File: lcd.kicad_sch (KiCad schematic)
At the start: 0 parts

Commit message: schema functionally done
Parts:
- added C18: 0.1uF, Capacitor_SMD:C_0805_2012Metric, symbol Device:C
- added C20: 1uF, Capacitor_SMD:C_0805_2012Metric, symbol Device:C
- added LCD1: LS013B7DH03, footprints:F3311A7H121010E200, symbol user:LS013B7DH03
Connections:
- new net: C20.1, LCD1.6 (VDDA), LCD1.7 (VDD), LCD1.8 (EXTMODE)
- new net: C18.1, LCD1.5 (DISP)
- new net GND: C18.2, C20.2, LCD1.10 (VSSA), LCD1.9 (VSS)
- new net LCD_COMIN: LCD1.4 (EXTCOMIN)
- new net LCD_SCLK: LCD1.1 (SCLK)
- new net LCD_SCS: LCD1.3 (SCS)
- new net LCD_SI: LCD1.2 (SI)
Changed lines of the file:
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@@
   (title_block
     (title "gkos pebble")
+    (date "2024-03-18")
+    (rev "1")
     (company "minteyay")
+    (comment 1 "memory LCD connection")
+  )
+  (junction (at 153.67 90.17) (diameter 0) (color 0 0 0 0)
+  )
+  (junction (at 157.48 121.92) (diameter 0) (color 0 0 0 0)
+  )
+  (junction (at 135.89 90.17) (diameter 0) (color 0 0 0 0)
+  )
+  (junction (at 135.89 121.92) (diameter 0) (color 0 0 0 0)
+  )
+  (junction (at 133.35 121.92) (diameter 0) (color 0 0 0 0)
+  )
+  (wire (pts (xy 133.35 90.17) (xy 135.89 90.17))
+    (stroke (width 0) (type default))
+  )
+  (wire (pts (xy 133.35 121.92) (xy 133.35 124.46))
+    (stroke (width 0) (type default))
+  )
+  (wire (pts (xy 153.67 107.95) (xy 149.86 107.95))
+    (stroke (width 0) (type default))
+  )
+  (wire (pts (xy 153.67 90.17) (xy 153.67 107.95))
+    (stroke (width 0) (type default))
+  )
+  (wire (pts (xy 106.68 107.95) (xy 119.38 107.95))
+    (stroke (width 0) (type default))
+  )
+  (wire (pts (xy 135.89 118.11) (xy 135.89 121.92))
+    (stroke (width 0) (type default))
+  )
+  (wire (pts (xy 133.35 118.11) (xy 133.35 121.92))
+    (stroke (width 0) (type default))
+  )
+  (wire (pts (xy 133.35 92.71) (xy 133.35 90.17))
+    (stroke (width 0) (type default))
+  )
+  (wire (pts (xy 157.48 109.22) (xy 157.48 90.17))
+    (stroke (width 0) (type default))
+  )
+  (wire (pts (xy 149.86 105.41) (xy 168.91 105.41))
+    (stroke (width 0) (type default))
+  )
+  (wire (pts (xy 157.48 90.17) (xy 153.67 90.17))
+    (stroke (width 0) (type default))
+  )
+  (wire (pts (xy 135.89 121.92) (xy 157.48 121.92))
+    (stroke (width 0) (type default))
+  )
+  (wire (pts (xy 157.48 121.92) (xy 157.48 116.84))
+    (stroke (width 0) (type default))
+  )
+  (wire (pts (xy 106.68 105.41) (xy 119.38 105.41))
+    (stroke (width 0) (type default))
+  )
+  (wire (pts (xy 168.91 116.84) (xy 168.91 121.92))
+    (stroke (width 0) (type default))
+  )
+  (wire (pts (xy 106.68 102.87) (xy 119.38 102.87))
+    (stroke (width 0) (type default))
+  )
+  (wire (pts (xy 149.86 102.87) (xy 175.26 102.87))
+    (stroke (width 0) (type default))
+  )
+  (wire (pts (xy 168.91 105.41) (xy 168.91 109.22))
+    (stroke (width 0) (type default))
+  )
+  (wire (pts (xy 133.35 121.92) (xy 135.89 121.92))
+    (stroke (width 0) (type default))
+  )
+  (wire (pts (xy 135.89 90.17) (xy 153.67 90.17))
+    (stroke (width 0) (type default))
+  )
+  (wire (pts (xy 157.48 121.92) (xy 168.91 121.92))
+    (stroke (width 0) (type default))
+  )
+  (wire (pts (xy 135.89 90.17) (xy 135.89 92.71))
+    (stroke (width 0) (type default))
+  )
+  (hierarchical_label "LCD_SCS" (shape input) (at 106.68 107.95 180) (fields_autoplaced)
+    (effects (font (size 1.27 1.27)) (justify right))
+  )
+  (hierarchical_label "LCD_SI" (shape input) (at 106.68 105.41 180) (fields_autoplaced)
+    (effects (font (size 1.27 1.27)) (justify right))
+  )
+  (hierarchical_label "LCD_SCLK" (shape input) (at 106.68 102.87 180) (fields_autoplaced)
+    (effects (font (size 1.27 1.27)) (justify right))
+  )
+  (hierarchical_label "LCD_COMIN" (shape input) (at 175.26 102.87 0) (fields_autoplaced)
+    (effects (font (size 1.27 1.27)) (justify left))
+  )
+  (symbol (lib_id "Device:C") (at 157.48 113.03 0) (unit 1)
+    (in_bom yes) (on_board yes) (dnp no)
+    (property "Reference" "C20" (at 160.02 111.76 0)
+      (effects (font (size 1.27 1.27)) (justify left))
+    )
+    (property "Value" "1uF" (at 160.02 114.3 0)
+      (effects (font (size 1.27 1.27)) (justify left))
+    )
+    (property "Footprint" "Capacitor_SMD:C_0805_2012Metric" (at 158.4452 116.84 0)
+      (effects (font (size 1.27 1.27)) hide)
+    )
+    (property "Datasheet" "~" (at 157.48 113.03 0)
+      (effects (font (size 1.27 1.27)) hide)
+    )
+    (pin "1")
+    (pin "2")
+    (instances
+      (project "gkos_pebble"
+        (path "/ab6fff6e-44fa-4992-ab9d-8d9a7df4367d/d83faf22-21bb-4089-b9cb-4974311e9f47"
+          (reference "C20") (unit 1)
+        )
+      )
+    )
+  )
+  (symbol (lib_id "user:LS013B7DH03") (at 134.62 105.41 0) (unit 1)
+    (in_bom yes) (on_board yes) (dnp no)
+    (property "Reference" "LCD1" (at 121.92 93.98 0)
+      (effects (font (size 1.27 1.27)) (justify left))
+    )
+    (property "Value" "LS013B7DH03" (at 138.43 116.84 0)
+      (effects (font (size 1.27 1.27)) (justify left))
+    )
+    (property "Footprint" "footprints:F3311A7H121010E200" (at 156.21 92.71 0)
+      (effects (font (size 1.27 1.27)) hide)
+    )
+    (property "Datasheet" "" (at 128.27 90.17 0)
+      (effects (font (size 1.27 1.27)) hide)
+    )
+    (pin "10")
+    (pin "9")
+    (pin "5")
+    (pin "6")
+    (pin "8")
+    (pin "7")
+    (pin "4")
+    (pin "3")
+    (pin "2")
+    (pin "1")
+    (instances
+      (project "gkos_pebble"
+        (path "/ab6fff6e-44fa-4992-ab9d-8d9a7df4367d/d83faf22-21bb-4089-b9cb-4974311e9f47"
+          (reference "LCD1") (unit 1)
+        )
+      )
+    )
+  )
+  (symbol (lib_id "Device:C") (at 168.91 113.03 0) (unit 1)
+    (in_bom yes) (on_board yes) (dnp no)
+    (property "Reference" "C18" (at 171.45 111.76 0)
+      (effects (font (size 1.27 1.27)) (justify left))
+    )
+    (property "Value" "0.1uF" (at 171.45 114.3 0)
+      (effects (font (size 1.27 1.27)) (justify left))
+    )
+    (property "Footprint" "Capacitor_SMD:C_0805_2012Metric" (at 169.8752 116.84 0)
+      (effects (font (size 1.27 1.27)) hide)
+    )
+    (property "Datasheet" "~" (at 168.91 113.03 0)
+      (effects (font (size 1.27 1.27)) hide)
+    )
+    (pin "1")
+    (pin "2")
+    (instances
+      (project "gkos_pebble"
+        (path "/ab6fff6e-44fa-4992-ab9d-8d9a7df4367d/d83faf22-21bb-4089-b9cb-4974311e9f47"
+          (reference "C18") (unit 1)
+        )
+      )
+    )
+  )
+  (symbol (lib_id "power:GND") (at 133.35 124.46 0) (unit 1)
+    (in_bom yes) (on_board yes) (dnp no)
+    (property "Reference" "#PWR052" (at 133.35 130.81 0)
+      (effects (font (size 1.27 1.27)) hide)
+    )
+    (property "Value" "GND" (at 133.35 128.27 0)
+      (effects (font (size 1.27 1.27)))
+    )
+    (property "Footprint" "" (at 133.35 124.46 0)
+      (effects (font (size 1.27 1.27)) hide)
+    )
+    (property "Datasheet" "" (at 133.35 124.46 0)
+      (effects (font (size 1.27 1.27)) hide)
+    )
+    (pin "1")
+    (instances
+      (project "gkos_pebble"
+        (path "/ab6fff6e-44fa-4992-ab9d-8d9a7df4367d/d83faf22-21bb-4089-b9cb-4974311e9f47"
+          (reference "#PWR052") (unit 1)
+        )
+      )
+    )
   )
 )

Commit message: reannotation
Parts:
- renumbered C20 to C40, C18 to C41
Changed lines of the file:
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@@
   (symbol (lib_id "Device:C") (at 157.48 113.03 0) (unit 1)
     (in_bom yes) (on_board yes) (dnp no)
-    (property "Reference" "C20" (at 160.02 111.76 0)
+    (property "Reference" "C40" (at 160.02 111.76 0)
       (effects (font (size 1.27 1.27)) (justify left))
     )
@@
       (project "gkos_pebble"
         (path "/ab6fff6e-44fa-4992-ab9d-8d9a7df4367d/d83faf22-21bb-4089-b9cb-4974311e9f47"
-          (reference "C20") (unit 1)
+          (reference "C40") (unit 1)
         )
       )
@@
   (symbol (lib_id "Device:C") (at 168.91 113.03 0) (unit 1)
     (in_bom yes) (on_board yes) (dnp no)
-    (property "Reference" "C18" (at 171.45 111.76 0)
+    (property "Reference" "C41" (at 171.45 111.76 0)
       (effects (font (size 1.27 1.27)) (justify left))
     )
@@
       (project "gkos_pebble"
         (path "/ab6fff6e-44fa-4992-ab9d-8d9a7df4367d/d83faf22-21bb-4089-b9cb-4974311e9f47"
-          (reference "C18") (unit 1)
+          (reference "C41") (unit 1)
         )
       )
@@
   (symbol (lib_id "power:GND") (at 133.35 124.46 0) (unit 1)
     (in_bom yes) (on_board yes) (dnp no)
-    (property "Reference" "#PWR052" (at 133.35 130.81 0)
+    (property "Reference" "#PWR087" (at 133.35 130.81 0)
       (effects (font (size 1.27 1.27)) hide)
     )
@@
       (project "gkos_pebble"
         (path "/ab6fff6e-44fa-4992-ab9d-8d9a7df4367d/d83faf22-21bb-4089-b9cb-4974311e9f47"
-          (reference "#PWR052") (unit 1)
+          (reference "#PWR087") (unit 1)
         )
       )

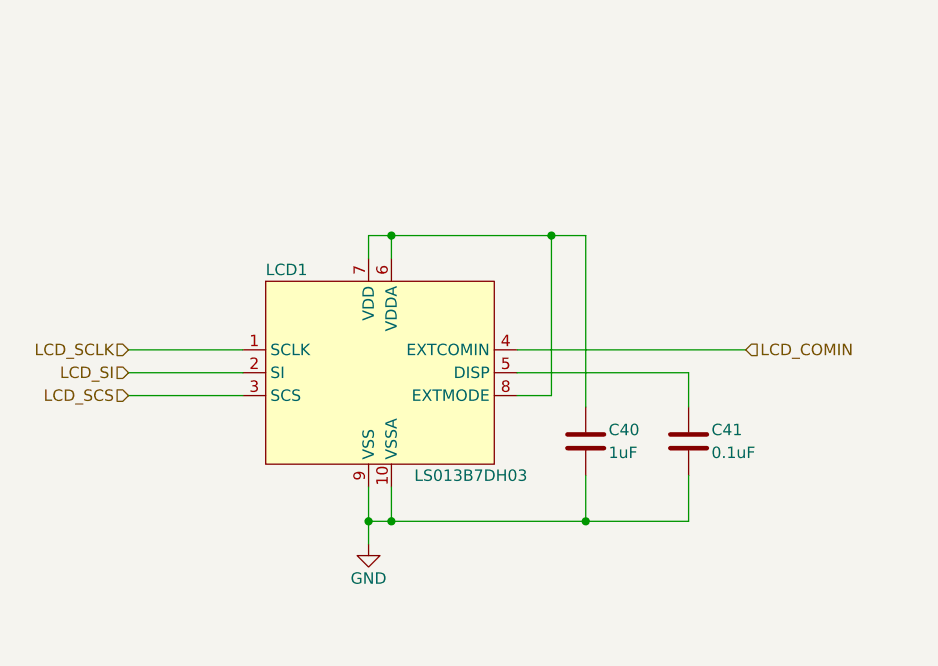
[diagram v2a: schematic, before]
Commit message: add external modules
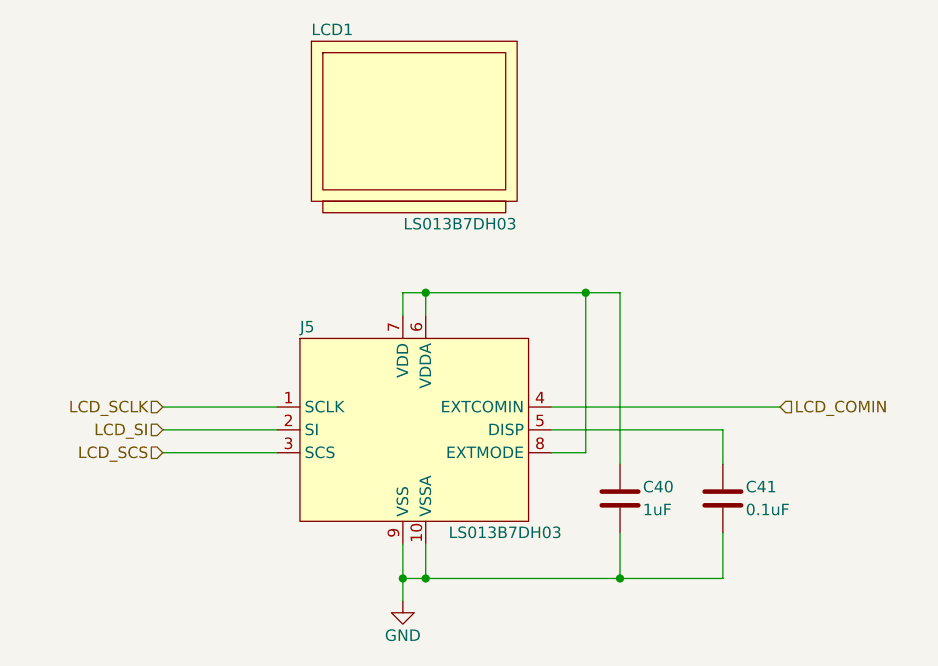
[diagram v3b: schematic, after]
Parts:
- added LCD1: LS013B7DH03, footprints:LS013B7DH03, symbol user:LS013B7DH03
- J5: renamed from LCD1; symbol user:LS013B7DH03 -> user:LS013B7DH03_CONN
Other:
- moved on the sheet: C40, C41, J5

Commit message: schematic cleanup
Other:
- moved on the sheet: C40, C41, J5, LCD1

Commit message: reannotate
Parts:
- renumbered C40 to C38, C41 to C39
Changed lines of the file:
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@@
   (symbol (lib_id "Device:C") (at 165.1 119.38 0) (mirror y) (unit 1)
     (in_bom yes) (on_board yes) (dnp no)
-    (property "Reference" "C40" (at 162.56 118.11 0)
+    (property "Reference" "C38" (at 162.56 118.11 0)
       (effects (font (size 1.27 1.27)) (justify left))
     )
@@
       (project "gkos_pebble"
         (path "/ab6fff6e-44fa-4992-ab9d-8d9a7df4367d/d83faf22-21bb-4089-b9cb-4974311e9f47"
-          (reference "C40") (unit 1)
+          (reference "C38") (unit 1)
         )
       )
@@
   (symbol (lib_id "Device:C") (at 176.53 119.38 0) (mirror y) (unit 1)
     (in_bom yes) (on_board yes) (dnp no)
-    (property "Reference" "C41" (at 173.99 118.11 0)
+    (property "Reference" "C39" (at 173.99 118.11 0)
       (effects (font (size 1.27 1.27)) (justify left))
     )
@@
       (project "gkos_pebble"
         (path "/ab6fff6e-44fa-4992-ab9d-8d9a7df4367d/d83faf22-21bb-4089-b9cb-4974311e9f47"
-          (reference "C41") (unit 1)
+          (reference "C39") (unit 1)
         )
       )
@@
   (symbol (lib_id "power:GND") (at 138.43 130.81 0) (unit 1)
     (in_bom yes) (on_board yes) (dnp no)
-    (property "Reference" "#PWR085" (at 138.43 137.16 0)
+    (property "Reference" "#PWR079" (at 138.43 137.16 0)
       (effects (font (size 1.27 1.27)) hide)
     )
@@
       (project "gkos_pebble"
         (path "/ab6fff6e-44fa-4992-ab9d-8d9a7df4367d/d83faf22-21bb-4089-b9cb-4974311e9f47"
-          (reference "#PWR085") (unit 1)
+          (reference "#PWR079") (unit 1)
         )
       )

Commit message: in progress pcb
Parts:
- C38, C39: footprint Capacitor_SMD:C_0805_2012Metric -> Capacitor_SMD:C_0603_1608Metric
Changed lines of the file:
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@@
       (effects (font (size 1.27 1.27)) (justify left))
     )
-    (property "Footprint" "Capacitor_SMD:C_0805_2012Metric" (at 164.1348 123.19 0)
+    (property "Footprint" "Capacitor_SMD:C_0603_1608Metric" (at 164.1348 123.19 0)
       (effects (font (size 1.27 1.27)) hide)
     )
@@
       (effects (font (size 1.27 1.27)) (justify left))
     )
-    (property "Footprint" "Capacitor_SMD:C_0805_2012Metric" (at 175.5648 123.19 0)
+    (property "Footprint" "Capacitor_SMD:C_0603_1608Metric" (at 175.5648 123.19 0)
       (effects (font (size 1.27 1.27)) hide)
     )
